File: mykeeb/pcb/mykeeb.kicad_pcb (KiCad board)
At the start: 2 copper layers, 84 parts, among them K0 KEYSW, K1 KEYSW, K10 KEYSW, K11 KEYSW, K12 KEYSW, K13 KEYSW, K14 KEYSW, K15 KEYSW, K16 KEYSW, K2 KEYSW, K20 KEYSW, K21 KEYSW, K22 KEYSW, K23 KEYSW, K24 KEYSW, K25 KEYSW, K26 KEYSW, K3 KEYSW, K30 KEYSW, K31 KEYSW, K32 KEYSW, K33 KEYSW, K34 KEYSW, K35 KEYSW, K36 KEYSW, K4 KEYSW, K40 KEYSW, K41 KEYSW, K42 KEYSW, K43 KEYSW, K44 KEYSW, K45 KEYSW, K46 KEYSW, K5 KEYSW, K6 KEYSW, SW1 SW_Push, U1 ProMicro, U2 ProMicro

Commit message: wip on mykeeb
Signed-off-by: Maximilian Huber <gh@maxhbr.de>
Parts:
- added BT1: Battery_Cell, Connector_JST:JST_PH_S2B-PH-K_1x02_P2.00mm_Horizontal, F.Cu at (183.0, 92.9)
- added K40b1: KEYSW, keyswitches:Kailh_socket_MX_optional_reversible, F.Cu at (85.7, 138.1)
- added K43b1: KEYSW, keyswitches:Kailh_socket_MX_optional_reversible, F.Cu at (104.8, 131.0)
- D0, D1, D10, D11, D12, D13, D14, D15, D16, D2, D20, D21, D22, D23, D24, D25, D26, D3, D30, D31, D32, D33, D34, D35, D36, D4, D40, D41, D42, D43, D44, D45, D46, D5, D6: footprint Keebio-Parts:Diode-Hybrid-Back -> Keebio-Parts:D_SOD123F
- H6, H7, H8: footprint MountingHole:MountingHole_3.2mm_M3 -> MountingHole:MountingHole_2.2mm_M2
- locked: renamed from H5; footprint MountingHole:MountingHole_3.2mm_M3 -> MountingHole:MountingHole_2.2mm_M2
- moved H1 228.4 mm to (42.9, 45.2)
- moved FID2 199.9 mm to (73.8, 42.9)
- moved H4 188.5 mm to (57.1, 142.9)
- moved H7 187.0 mm to (76.2, 83.3)
- moved FID1 166.2 mm to (95.2, 128.6)
- moved locked 129.8 mm to (119.1, 111.9)
- moved H2 123.5 mm to (171.4, 40.5)
- moved H6 122.6 mm to (133.3, 71.4)
- moved FID3 119.2 mm to (161.9, 83.3)
- moved H3 80.0 mm to (190.5, 104.8)
- moved H8 72.4 mm to (169.1, 123.8)
- moved SW1 38.7 mm to (181.5, 43.2), turned to 0 degrees
- moved D36 29.8 mm to (188.1, 109.5), turned to -30 degrees
- moved locked 25.8 mm to (183.4, 119.1), turned to -30 degrees
- moved D26 25.6 mm to (171.4, 100.0), turned to -90 degrees
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- renumbered K41 to locked, K36 to locked, K42 to locked, K43 to locked
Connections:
- net +5V renamed GND
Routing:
- net col0: track 0.00 -> 348.8 mm
- net col1: track 0.00 -> 279.4 mm
- net col3: track 0.00 -> 258.1 mm
- net row4: track 0.00 -> 252.1 mm, vias 0 -> 2
- net col2: track 0.00 -> 250.4 mm
- net col4: track 0.00 -> 219.5 mm
- net row3: track 0.00 -> 213.9 mm
- net col5: track 0.00 -> 200.0 mm
- net row2: track 0.00 -> 196.6 mm
- net col6: track 0.00 -> 184.4 mm
- net row1: track 0.00 -> 178.1 mm
- net row0: track 0.00 -> 168.9 mm
- net GND: track 0.00 -> 102.2 mm
- net Net-(D40-Pad1): track 0.00 -> 91.1 mm
- net Bat+: track 0.00 -> 81.1 mm
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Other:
- board outline added: 161.9 x 126.2 mm

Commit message: wip on mykeeb
Signed-off-by: Maximilian Huber <gh@maxhbr.de>
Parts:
- H2, H6, H7: value MountingHole -> locked
- moved D46 43.1 mm to (135.7, 126.2), turned to -90 degrees
- moved D45 20.9 mm to (138.1, 126.2), turned to -90 degrees
- moved D36 15.1 mm to (173.8, 104.8), turned to -90 degrees
- moved BT1 9.73 mm to (182.8, 102.6)
- moved H2 1.61 mm to (172.4, 39.2)
- moved D24 0.98 mm to (133.3, 83.3)
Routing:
- net Net-(D46-Pad1): track 27.8 -> 74.2 mm
- net row4: track 252.1 -> 207.0 mm, vias 2 -> 0
- net row3: track 213.9 -> 196.0 mm
- net Net-(D45-Pad1): track 26.3 -> 42.8 mm
- net RST: track 38.5 -> 24.7 mm
- net Net-(D36-Pad1): track 33.8 -> 43.0 mm, vias 1 -> 0
- net GND: track 102.2 -> 109.7 mm
- net col1: track 279.4 -> 272.6 mm
- net col6: track 184.4 -> 190.3 mm
- net col3: track 258.1 -> 253.5 mm
- net col0: track 348.8 -> 344.6 mm
- net row2: track 196.6 -> 192.9 mm
- net Net-(D26-Pad1): track 32.1 -> 28.5 mm
- net Bat+: track 81.1 -> 84.4 mm
- net Net-(D40-Pad1): track 91.1 -> 94.3 mm
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
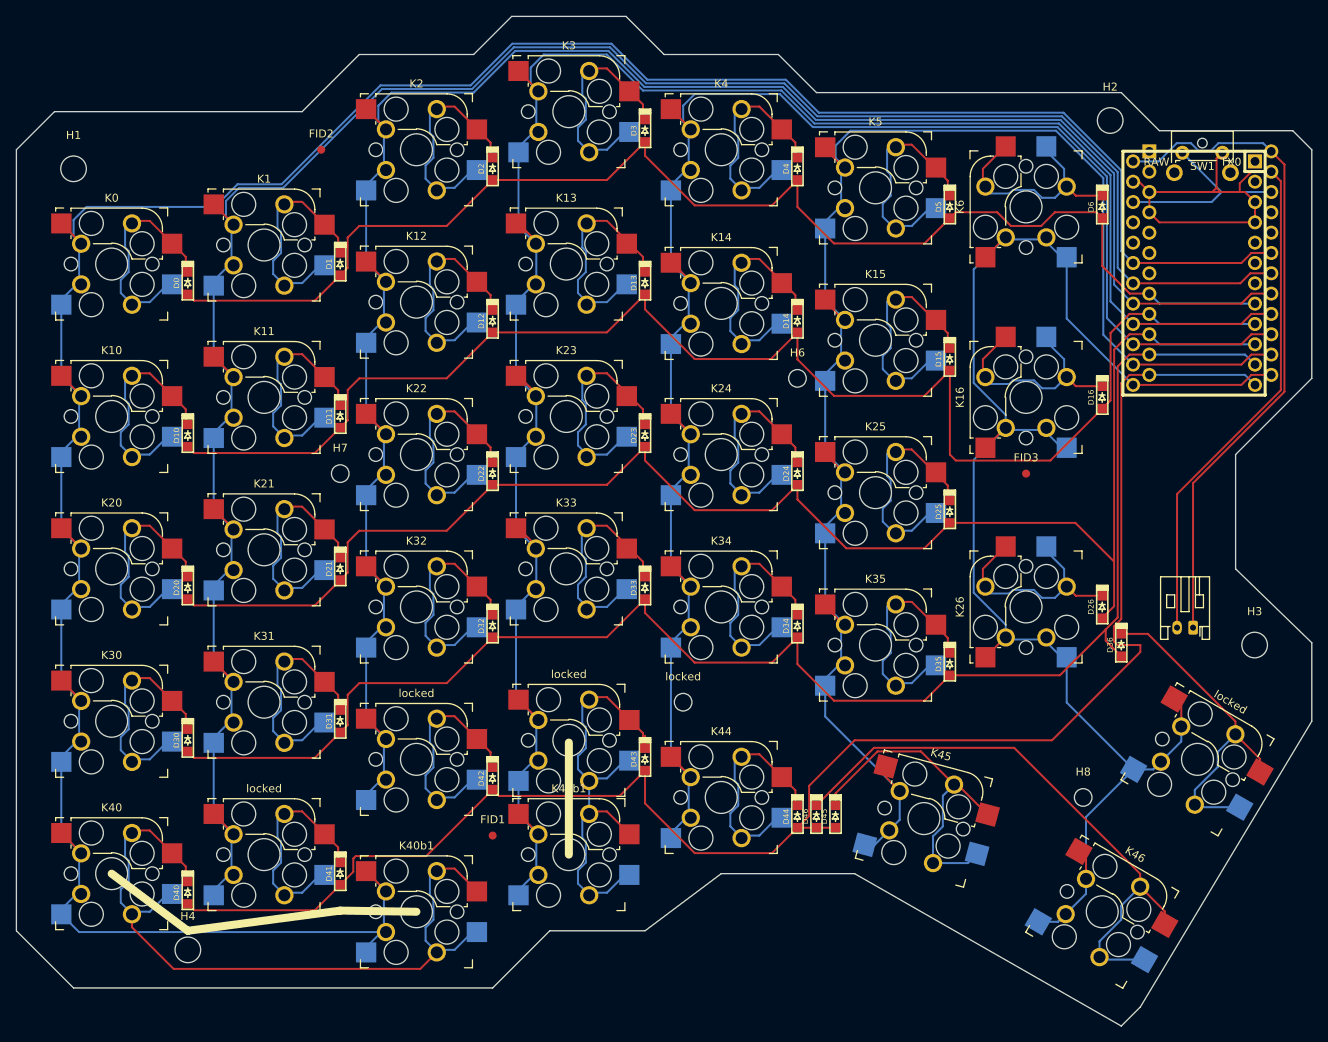
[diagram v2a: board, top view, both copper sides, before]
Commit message: add v0.1 pcb
Signed-off-by: Maximilian Huber <gh@maxhbr.de>
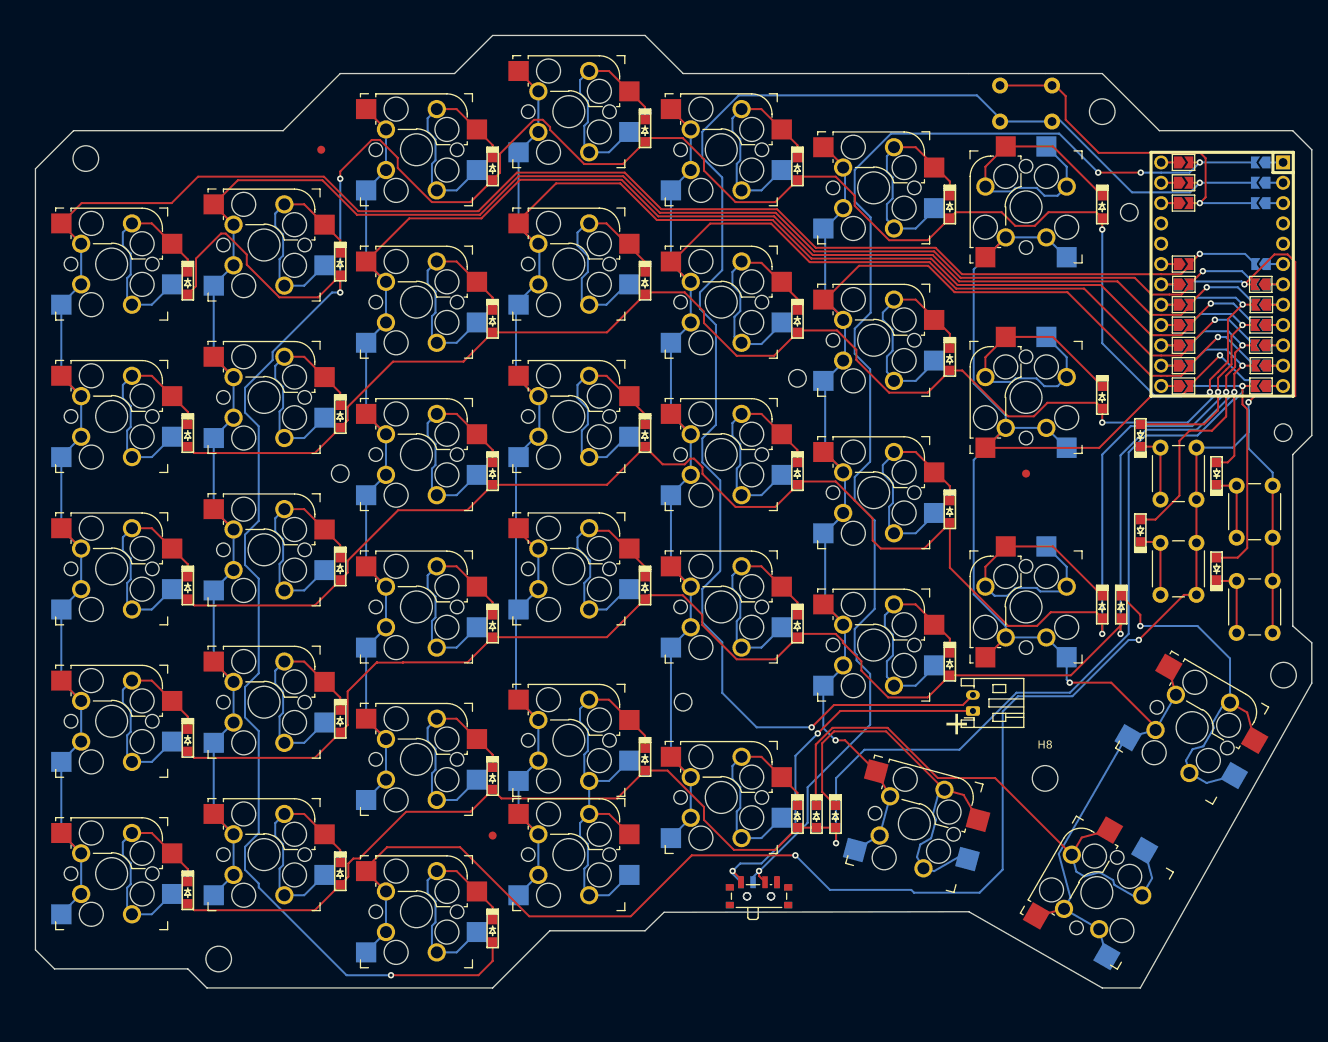
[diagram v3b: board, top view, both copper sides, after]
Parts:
- removed K40b1: KEYSW, keyswitches:Kailh_socket_MX_optional_reversible
- removed U2: ProMicro, Keebio-Parts:ArduinoProMicro-BackSide
- added D17: DIODE, Keebio-Parts:D_SOD123F, F.Cu at (176.2, 78.6)
- added D27: DIODE, Keebio-Parts:D_SOD123F, F.Cu at (176.2, 90.5)
- added D37: DIODE, Keebio-Parts:D_SOD123F, F.Cu at (185.7, 83.3)
- added D47: DIODE, Keebio-Parts:D_SOD123F, F.Cu at (185.7, 95.2)
- added D7: DIODE, Keebio-Parts:D_SOD123F, F.Cu at (95.2, 140.5)
- added H10: MountingHole, MountingHole:MountingHole_2.2mm_M2, F.Cu at (194.1, 78.2)
- added H9: MountingHole, MountingHole:MountingHole_2.2mm_M2, F.Cu at (174.8, 50.7)
- added JPbat+a0: SolderJumper_2_Open, Jumper:SolderJumper-2_P1.3mm_Open_TrianglePad1.0x1.5mm, F.Cu at (181.6, 44.5)
- added JPbat+b0: SolderJumper_2_Open, Jumper:SolderJumper-2_P1.3mm_Open_TrianglePad1.0x1.5mm, B.Cu at (191.3, 44.5)
- added JPc0a1: SolderJumper_2_Open, Jumper:SolderJumper-2_P1.3mm_Open_TrianglePad1.0x1.5mm, F.Cu at (181.6, 57.1)
- added JPc0b1: SolderJumper_2_Open, Jumper:SolderJumper-2_P1.3mm_Open_TrianglePad1.0x1.5mm, B.Cu at (191.3, 57.1)
- added JPc1a1: SolderJumper_2_Open, Jumper:SolderJumper-2_P1.3mm_Open_TrianglePad1.0x1.5mm, F.Cu at (181.6, 59.7)
- added JPc1b1: SolderJumper_2_Open, Jumper:SolderJumper-2_P1.3mm_Open_TrianglePad1.0x1.5mm, B.Cu at (191.3, 59.7)
- added JPc2a1: SolderJumper_2_Open, Jumper:SolderJumper-2_P1.3mm_Open_TrianglePad1.0x1.5mm, F.Cu at (181.6, 62.2)
- added JPc2b1: SolderJumper_2_Open, Jumper:SolderJumper-2_P1.3mm_Open_TrianglePad1.0x1.5mm, B.Cu at (191.3, 62.2)
- added JPc3a1: SolderJumper_2_Open, Jumper:SolderJumper-2_P1.3mm_Open_TrianglePad1.0x1.5mm, F.Cu at (181.6, 64.8)
- added JPc3b1: SolderJumper_2_Open, Jumper:SolderJumper-2_P1.3mm_Open_TrianglePad1.0x1.5mm, B.Cu at (191.3, 64.8)
- added JPc4a1: SolderJumper_2_Open, Jumper:SolderJumper-2_P1.3mm_Open_TrianglePad1.0x1.5mm, F.Cu at (181.6, 67.3)
- added JPc4b1: SolderJumper_2_Open, Jumper:SolderJumper-2_P1.3mm_Open_TrianglePad1.0x1.5mm, B.Cu at (191.3, 67.3)
- added JPc5a1: SolderJumper_2_Open, Jumper:SolderJumper-2_P1.3mm_Open_TrianglePad1.0x1.5mm, F.Cu at (181.6, 69.8)
- added JPc5b1: SolderJumper_2_Open, Jumper:SolderJumper-2_P1.3mm_Open_TrianglePad1.0x1.5mm, B.Cu at (191.3, 69.8)
- added JPc6a1: SolderJumper_2_Open, Jumper:SolderJumper-2_P1.3mm_Open_TrianglePad1.0x1.5mm, F.Cu at (181.6, 72.4)
- added JPc6b1: SolderJumper_2_Open, Jumper:SolderJumper-2_P1.3mm_Open_TrianglePad1.0x1.5mm, B.Cu at (191.3, 72.4)
- added JPc7a1: SolderJumper_2_Open, Jumper:SolderJumper-2_P1.3mm_Open_TrianglePad1.0x1.5mm, F.Cu at (191.3, 59.7)
- added JPc7b1: SolderJumper_2_Open, Jumper:SolderJumper-2_P1.3mm_Open_TrianglePad1.0x1.5mm, B.Cu at (181.6, 59.7)
- added JPgbda0: SolderJumper_2_Open, Jumper:SolderJumper-2_P1.3mm_Open_TrianglePad1.0x1.5mm, F.Cu at (181.6, 47.0)
- added JPgndb0: SolderJumper_2_Open, Jumper:SolderJumper-2_P1.3mm_Open_TrianglePad1.0x1.5mm, B.Cu at (191.3, 47.0)
- added JPr0a1: SolderJumper_2_Open, Jumper:SolderJumper-2_P1.3mm_Open_TrianglePad1.0x1.5mm, F.Cu at (191.3, 62.2)
- added JPr0b1: SolderJumper_2_Open, Jumper:SolderJumper-2_P1.3mm_Open_TrianglePad1.0x1.5mm, B.Cu at (181.6, 62.2)
- added JPr1a1: SolderJumper_2_Open, Jumper:SolderJumper-2_P1.3mm_Open_TrianglePad1.0x1.5mm, F.Cu at (191.3, 64.8)
- added JPr1b1: SolderJumper_2_Open, Jumper:SolderJumper-2_P1.3mm_Open_TrianglePad1.0x1.5mm, B.Cu at (181.6, 64.8)
- added JPr2a1: SolderJumper_2_Open, Jumper:SolderJumper-2_P1.3mm_Open_TrianglePad1.0x1.5mm, F.Cu at (191.3, 67.3)
- added JPr2b1: SolderJumper_2_Open, Jumper:SolderJumper-2_P1.3mm_Open_TrianglePad1.0x1.5mm, B.Cu at (181.6, 67.3)
- added JPr3a1: SolderJumper_2_Open, Jumper:SolderJumper-2_P1.3mm_Open_TrianglePad1.0x1.5mm, F.Cu at (191.3, 69.8)
- added JPr3b1: SolderJumper_2_Open, Jumper:SolderJumper-2_P1.3mm_Open_TrianglePad1.0x1.5mm, B.Cu at (181.6, 69.8)
- added JPr4a1: SolderJumper_2_Open, Jumper:SolderJumper-2_P1.3mm_Open_TrianglePad1.0x1.5mm, F.Cu at (191.3, 72.4)
- added JPr4b1: SolderJumper_2_Open, Jumper:SolderJumper-2_P1.3mm_Open_TrianglePad1.0x1.5mm, B.Cu at (181.6, 72.4)
- added JPresa0: SolderJumper_2_Open, Jumper:SolderJumper-2_P1.3mm_Open_TrianglePad1.0x1.5mm, F.Cu at (181.6, 49.5)
- added JPresb0: SolderJumper_2_Open, Jumper:SolderJumper-2_P1.3mm_Open_TrianglePad1.0x1.5mm, B.Cu at (191.3, 49.5)
- added K17: KEYSW, Button_Switch_THT:SW_PUSH_6mm_H8mm, F.Cu at (183.2, 80.1)
- added K27: KEYSW, Button_Switch_THT:SW_PUSH_6mm_H8mm, F.Cu at (183.2, 92.0)
- added K37: KEYSW, Button_Switch_THT:SW_PUSH_6mm_H8mm, F.Cu at (192.8, 84.9)
- added K47: KEYSW, Button_Switch_THT:SW_PUSH_6mm_H8mm, F.Cu at (192.8, 96.8)
- added K7: KEYSW, mykeeb:Kailh_socket_MX_optional_reversible_1u, F.Cu at (85.7, 138.1)
- added SWbat1: SW_SPST, Button_Switch_SMD:SW_SPDT_PCM12, F.Cu at (128.5, 135.8)
- added SWbat2: SW_SPST, Button_Switch_SMD:SW_SPDT_PCM12, B.Cu at (128.5, 135.8)
- H8: footprint MountingHole:MountingHole_2.2mm_M2 -> MountingHole:MountingHole_3.2mm_M3
- K0, K1, K10, K11, K12, K13, K14, K15, K2, K20, K21, K22, K23, K24, K25, K3, K30, K31, K32, K33, K34, K35, K4, K40, K43b1, K44, K5, locked (x3): footprint keyswitches:Kailh_socket_MX_optional_reversible -> mykeeb:Kailh_socket_MX_optional_reversible_1u
- K16, K45, K6: footprint keyswitches:Kailh_socket_MX_optional_reversible -> mykeeb:Kailh_socket_MX_optional_reversible_1.25u
- K26, K46: footprint keyswitches:Kailh_socket_MX_optional_reversible -> mykeeb:Kailh_socket_MX_optional_reversible_1.5u
- K36: renamed from locked; footprint keyswitches:Kailh_socket_MX_optional_reversible -> mykeeb:Kailh_socket_MX_optional_reversible_1u
- SW1: footprint Keebio-Parts:SW_Tactile_SPST_Angled_MJTP1117 -> Button_Switch_THT:SW_PUSH_6mm; moved to B.Cu
- moved BT1 29.4 mm to (155.3, 113.0), turned to 90 degrees
- moved SW1 18.3 mm to (165.2, 34.8), turned to 180 degrees
- moved H8 5.32 mm to (164.3, 121.4)
- moved H3 5.21 mm to (194.1, 108.5)
- moved D36 4.76 mm to (173.8, 100.0)
- moved H4 4.02 mm to (61.0, 144.0)
- moved K36 4.02 mm to (182.7, 115.1)
- moved U1 3.51 mm to (186.4, 58.4)
- moved K46 2.48 mm to (170.8, 135.7), turned to 60 degrees
- moved H1 2.00 mm to (44.4, 44.0)
- moved H2 1.49 mm to (171.4, 38.1)
- moved K45 1.36 mm to (148.0, 127.1)
- moved K13 0.32 mm to (104.8, 57.1)
- moved K23 0.32 mm to (104.8, 76.2)
- moved K33 0.32 mm to (104.8, 95.2)
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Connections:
- BT1 pad 1: Bat+ -> Net-(BT1-Pad1)
- U1 pad 1: unconnected-(U1-Pad1) -> Net-(JPbat+b0-Pad1)
- U1 pad 10: row2 -> c4b
- U1 pad 11: row3 -> c5b
- U1 pad 12: row4 -> c6b
- U1 pad 13: col6 -> c6a
- U1 pad 14: col5 -> c5a
- U1 pad 15: col4 -> c4a
- U1 pad 16: col3 -> c3a
- U1 pad 17: col2 -> c2a
- U1 pad 18: col1 -> c1a
- U1 pad 19: col0 -> c0a
- U1 pad 2: unconnected-(U1-Pad2) -> Net-(JPgndb0-Pad1)
- U1 pad 22: RST -> Net-(JPresa0-Pad1)
- U1 pad 23: GND -> Net-(JPgbda0-Pad1)
- U1 pad 24: Bat+ -> Net-(JPbat+a0-Pad1)
- U1 pad 3: GND -> Net-(JPresb0-Pad1)
- U1 pad 4: GND -> unconnected-(U1-Pad4)
- U1 pad 6: unconnected-(U1-Pad6) -> c0b
- U1 pad 7: unconnected-(U1-Pad7) -> c1b
- U1 pad 8: row0 -> c2b
- U1 pad 9: row1 -> c3b
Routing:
- net col7: track 0.00 -> 252.0 mm, vias 0 -> 4
- net row0: track 166.3 -> 345.1 mm, vias 0 -> 6
- net GND: track 109.7 -> 189.7 mm, vias 0 -> 2
- net Bat+: track 84.4 -> 158.7 mm, vias 0 -> 4
- net col0: track 344.6 -> 273.3 mm, vias 0 -> 1
- net Net-(D40-Pad1): track 94.3 -> 28.0 mm
- net Net-(BT1-Pad1): track 0.00 -> 47.4 mm, vias 0 -> 2
- net row2: track 192.9 -> 227.8 mm, vias 0 -> 3
- net Net-(D7-Pad1): track 0.00 -> 28.0 mm
- net col5: track 198.9 -> 177.5 mm, vias 0 -> 2
- net RST: track 24.7 -> 44.9 mm, vias 0 -> 1
- net col1: track 272.6 -> 254.3 mm, vias 0 -> 1
- net row4: track 207.0 -> 224.6 mm, vias 0 -> 2
- net col4: track 217.0 -> 200.9 mm, vias 0 -> 1
- net col2: track 250.5 -> 235.7 mm, vias 0 -> 1
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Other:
- board size 161.9 x 126.2 mm -> 159.5 x 119.1 mm
- board text added: "+"

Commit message: wip on mykeeb
Signed-off-by: Maximilian Huber <gh@maxhbr.de>
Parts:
- moved H6 1.00 mm to (132.3, 71.4)
- moved H7 1.00 mm to (75.2, 83.3)
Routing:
- net col7: track 252.0 -> 248.0 mm
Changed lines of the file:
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@@
     (property "Sheetname" "")
     (attr exclude_from_pos_files)
-    (fp_text reference "H8" (at 0 -4.2) (layer "F.SilkS")
+    (fp_text reference "H8" (at 0 -4.2) (layer "F.SilkS") hide
       (effects (font (size 1 1) (thickness 0.15)))
     )
@@
   )
   (footprint "MountingHole:MountingHole_2.2mm_M2" locked (layer "F.Cu")
-    (at 76.2 83.34375)
+    (at 75.2 83.34375)
     (descr "Mounting Hole 2.2mm, no annular, M2")
     (tags "mounting hole 2.2mm no annular m2")
@@
   )
   (footprint "MountingHole:MountingHole_2.2mm_M2" locked (layer "F.Cu")
-    (at 133.35 71.4375)
+    (at 132.35 71.4375)
     (descr "Mounting Hole 2.2mm, no annular, M2")
     (tags "mounting hole 2.2mm no annular m2")
@@
   (via locked (at 188.976 72.39) (size 0.8) (drill 0.4) (layers "F.Cu" "B.Cu") (net 12))
   (via (at 138.176 129.54) (size 0.8) (drill 0.4) (layers "F.Cu" "B.Cu") (net 12))
-  (segment (start 174.752 80.677468) (end 174.752 103.386614) (width 0.25) (layer "B.Cu") (net 12))
-  (segment (start 183.35625 78.58125) (end 176.848218 78.58125) (width 0.25) (layer "B.Cu") (net 12))
+  (segment (start 176.848218 78.58125) (end 174.752 80.677468) (width 0.25) (layer "B.Cu") (net 12))
+  (segment (start 187.892193 74.045307) (end 183.35625 78.58125) (width 0.25) (layer "B.Cu") (net 12))
+  (segment (start 174.752 103.386614) (end 160.282614 117.856) (width 0.25) (layer "B.Cu") (net 12))
   (segment (start 188.976 73.160614) (end 188.091307 74.045307) (width 0.25) (layer "B.Cu") (net 12))
+  (segment (start 138.176 121.412) (end 138.176 129.54) (width 0.25) (layer "B.Cu") (net 12))
+  (segment (start 160.282614 117.856) (end 141.732 117.856) (width 0.25) (layer "B.Cu") (net 12))
   (segment (start 188.091307 74.045307) (end 187.892193 74.045307) (width 0.25) (layer "B.Cu") (net 12))
   (segment locked (start 182.335 72.39) (end 188.976 72.39) (width 0.25) (layer "B.Cu") (net 12))
   (segment (start 188.976 72.39) (end 188.976 73.160614) (width 0.25) (layer "B.Cu") (net 12))
-  (segment (start 174.752 103.386614) (end 167.410489 110.728125) (width 0.25) (layer "B.Cu") (net 12))
-  (segment (start 187.892193 74.045307) (end 183.35625 78.58125) (width 0.25) (layer "B.Cu") (net 12))
-  (segment (start 138.176 121.412) (end 138.176 129.54) (width 0.25) (layer "B.Cu") (net 12))
-  (segment (start 176.848218 78.58125) (end 174.752 80.677468) (width 0.25) (layer "B.Cu") (net 12))
-  (segment (start 160.734375 110.728125) (end 153.6065 117.856) (width 0.25) (layer "B.Cu") (net 12))
   (segment (start 141.732 117.856) (end 138.176 121.412) (width 0.25) (layer "B.Cu") (net 12))
-  (segment (start 167.410489 110.728125) (end 160.734375 110.728125) (width 0.25) (layer "B.Cu") (net 12))
-  (segment (start 153.6065 117.856) (end 141.732 117.856) (width 0.25) (layer "B.Cu") (net 12))
+  (segment (start 174.752 80.677468) (end 174.752 103.386614) (width 0.25) (layer "B.Cu") (net 12))
+  (segment (start 183.35625 78.58125) (end 176.848218 78.58125) (width 0.25) (layer "B.Cu") (net 12))
   (segment (start 41.335 109.22) (end 41.335 109.28) (width 0.25) (layer "F.Cu") (net 13))
   (segment (start 116.332 50.292) (end 111.76 45.72) (width 0.25) (layer "F.Cu") (net 13))
@@
   (via (at 176.022 104.14) (size 0.8) (drill 0.4) (layers "F.Cu" "B.Cu") (net 74))
   (via (at 189.23 59.69) (size 0.8) (drill 0.4) (layers "F.Cu" "B.Cu") (net 74))
-  (segment (start 159.004 132.842) (end 156.11475 135.73125) (width 0.25) (layer "B.Cu") (net 74))
   (segment (start 81.915 140.6525) (end 79.435 143.1325) (width 0.25) (layer "B.Cu") (net 74))
-  (segment (start 147.574 135.382) (end 137.414 135.382) (width 0.25) (layer "B.Cu") (net 74))
-  (segment (start 188.867989 59.327989) (end 182.697011 59.327989) (width 0.25) (layer "B.Cu") (net 74))
-  (segment (start 160.920573 111.177645) (end 159.004 113.094218) (width 0.25) (layer "B.Cu") (net 74))
+  (segment (start 156.11475 135.73125) (end 147.92325 135.73125) (width 0.25) (layer "B.Cu") (net 74))
+  (segment (start 159.004 132.842) (end 156.11475 135.73125) (width 0.25) (layer "B.Cu") (net 74))
+  (segment (start 176.022 104.14) (end 174.752 104.14) (width 0.25) (layer "B.Cu") (net 74))
+  (segment (start 174.752 104.14) (end 159.004 119.888) (width 0.25) (layer "B.Cu") (net 74))
+  (segment (start 159.004 119.888) (end 159.004 132.842) (width 0.25) (layer "B.Cu") (net 74))
   (segment (start 147.92325 135.73125) (end 147.574 135.382) (width 0.25) (layer "B.Cu") (net 74))
+  (segment (start 188.867989 59.327989) (end 182.697011 59.327989) (width 0.25) (layer "B.Cu") (net 74))
   (segment (start 192.75 83.2125) (end 189.738 80.2005) (width 0.25) (layer "B.Cu") (net 74))
-  (segment (start 137.414 135.382) (end 133.096 131.064) (width 0.25) (layer "B.Cu") (net 74))
+  (segment (start 147.574 135.382) (end 137.414 135.382) (width 0.25) (layer "B.Cu") (net 74))
   (segment (start 79.435 143.1325) (end 79.435 143.1925) (width 0.25) (layer "B.Cu") (net 74))
+  (segment (start 137.414 135.382) (end 133.096 131.064) (width 0.25) (layer "B.Cu") (net 74))
   (segment (start 189.738 75.438) (end 189.738 74.422) (width 0.25) (layer "B.Cu") (net 74))
-  (segment (start 176.022 104.14) (end 174.752 104.14) (width 0.25) (layer "B.Cu") (net 74))
   (segment (start 192.75 84.85625) (end 192.75 83.2125) (width 0.25) (layer "B.Cu") (net 74))
-  (segment (start 167.714355 111.177645) (end 160.920573 111.177645) (width 0.25) (layer "B.Cu") (net 74))
   (segment (start 189.738 75.438) (end 189.738 78.152625) (width 0.25) (layer "B.Cu") (net 74))
-  (segment (start 156.11475 135.73125) (end 147.92325 135.73125) (width 0.25) (layer "B.Cu") (net 74))
   (segment (start 187.796875 80.09375) (end 183.225 80.09375) (width 0.25) (layer "B.Cu") (net 74))
   (segment (start 81.915 135.5725) (end 81.915 140.6525) (width 0.25) (layer "B.Cu") (net 74))
@@
   (segment (start 189.738 80.2005) (end 189.738 75.438) (width 0.25) (layer "B.Cu") (net 74))
   (segment (start 182.697011 59.327989) (end 182.335 59.69) (width 0.25) (layer "B.Cu") (net 74))
-  (segment (start 159.004 113.094218) (end 159.004 132.842) (width 0.25) (layer "B.Cu") (net 74))
-  (segment (start 174.752 104.14) (end 167.714355 111.177645) (width 0.25) (layer "B.Cu") (net 74))
   (segment (start 95.25 139.09375) (end 95.25 137.5375) (width 0.25) (layer "F.Cu") (net 77))
   (segment (start 95.25 137.5375) (end 93.285 135.5725) (width 0.25) (layer "F.Cu") (net 77))

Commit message: WIP
Signed-off-by: Maximilian Huber <gh@maxhbr.de>
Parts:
- removed K43b1: KEYSW, mykeeb:Kailh_socket_MX_optional_reversible_1u
- locked: footprint MountingHole:MountingHole_2.2mm_M2 -> MountingHole:MountingHole_3.2mm_M3
- moved H2 35.7 mm to (135.7, 36.9)
- moved locked 14.3 mm to (104.8, 131.0)
- moved D43 14.1 mm to (114.3, 133.1)
- moved locked 7.14 mm to (111.9, 111.9)
- moved FID3 4.76 mm to (157.2, 83.3)
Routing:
- net Net-(D43-Pad1): track 55.7 -> 27.7 mm
- net col3: track 245.7 -> 220.9 mm
- net row4: track 224.6 -> 229.2 mm
- net GND: track 189.7 -> 192.4 mm
- net RST: track 44.9 -> 46.5 mm
- net col7: track 248.0 -> 247.4 mm
- net Bat+: track 158.7 -> 158.2 mm, vias 4 -> 3
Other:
- outline, holes or cut-outs redrawn
